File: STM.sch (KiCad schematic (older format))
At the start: 14 parts, among them J3 Micro_SD_Card_Det, J4 TagConnect_TC2030_SWD, Q9 AO3401A, SW8 POWER, U8 STM32L151C8Tx

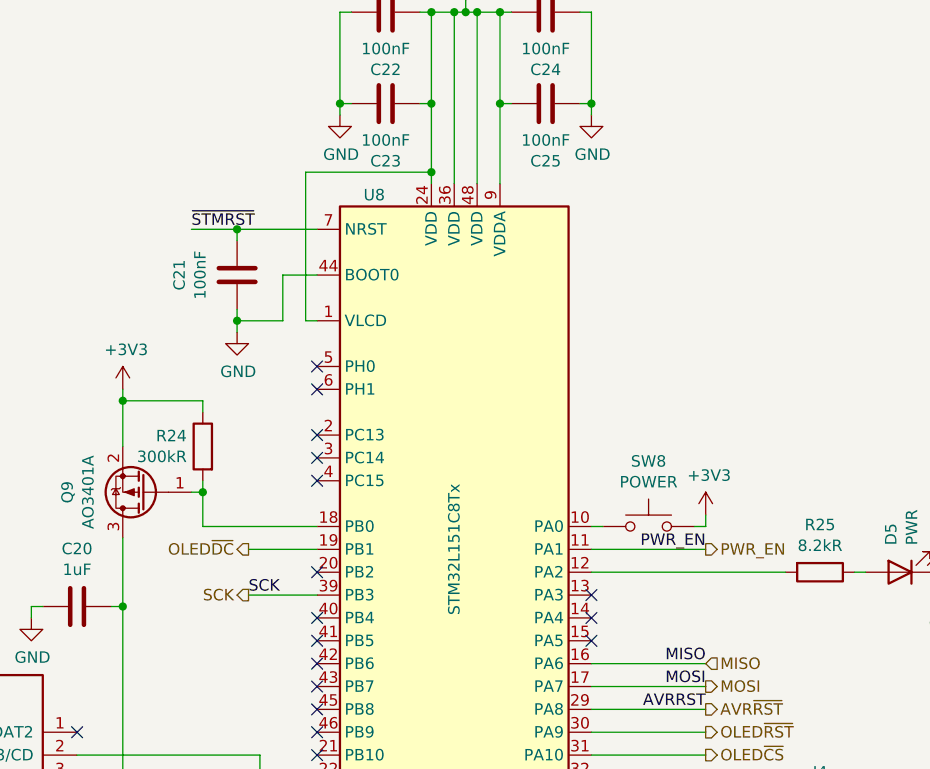
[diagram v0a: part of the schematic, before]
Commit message: Add charge state/current sensing and VBUS wakeup source
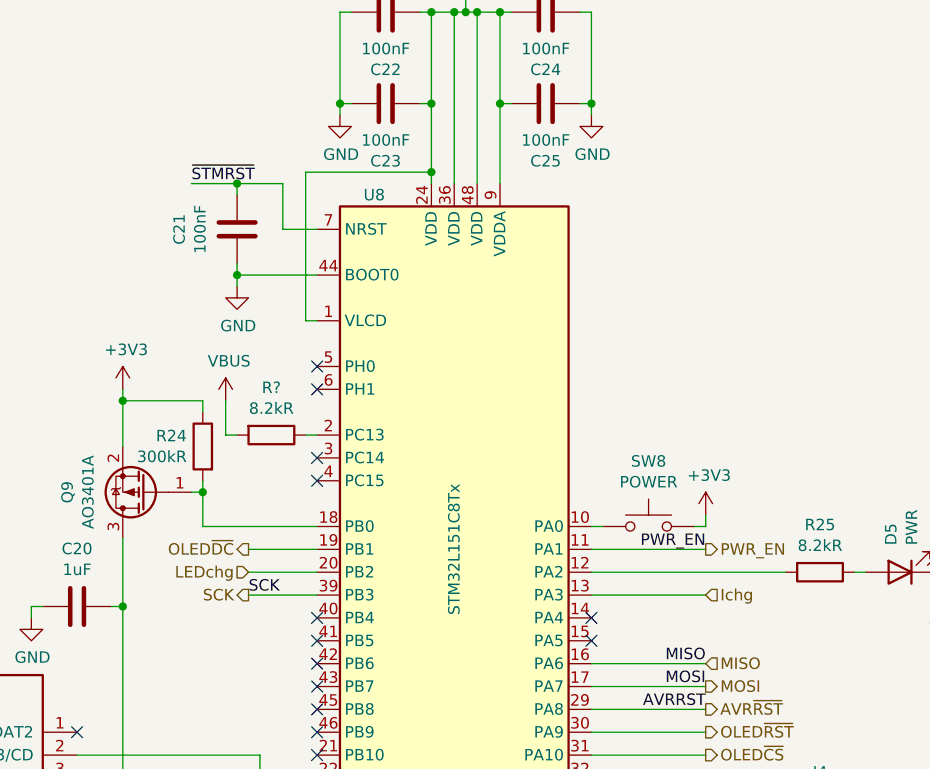
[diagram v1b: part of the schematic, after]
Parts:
- added R?: 8.2kR, Resistor_SMD:R_0402_1005Metric, symbol Device:R
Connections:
- net Ichg: now reaches U8.13 (PA3)
- net at U8.2 (PC13): now also R?.1
- net LEDchg: now reaches U8.20 (PB2)
- new net VBUS: R?.2
- no-connect marks 22 -> 19
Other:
- moved on the sheet: C21
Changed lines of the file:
@@
 L Device:C C?
 U 1 1 60D10135
-P 5100 2700
+P 5100 2500
 AR Path="/60D10135" Ref="C?"  Part="1"
 AR Path="/6051E9DC/60D10135" Ref="C?"  Part="1"
 AR Path="/60CF39C0/60D10135" Ref="C21"  Part="1"
-F 0 "C21" V 5352 2700 50  0000 C CNN
-F 1 "100nF" V 5261 2700 50  0000 C CNN
-F 2 "Capacitor_SMD:C_0402_1005Metric" H 5138 2550 50  0001 C CNN
-F 3 "~" H 5100 2700 50  0001 C CNN
-F 4 "C1525" H 5100 2700 50  0001 C CNN "LCSC"
-	1    5100 2700
+F 0 "C21" V 5352 2500 50  0000 C CNN
+F 1 "100nF" V 5261 2500 50  0000 C CNN
+F 2 "Capacitor_SMD:C_0402_1005Metric" H 5138 2350 50  0001 C CNN
+F 3 "~" H 5100 2500 50  0001 C CNN
+F 4 "C1525" H 5100 2500 50  0001 C CNN "LCSC"
+	1    5100 2500
 	-1   0    0    1
 $EndComp
@@
 L power:GND #PWR?
 U 1 1 60D1013B
-P 5100 2950
+P 5100 2750
 AR Path="/6051E9DC/60D1013B" Ref="#PWR?"  Part="1"
 AR Path="/60CF39C0/60D1013B" Ref="#PWR0105"  Part="1"
-F 0 "#PWR0105" H 5100 2700 50  0001 C CNN
-F 1 "GND" H 5105 2777 50  0000 C CNN
-F 2 "" H 5100 2950 50  0001 C CNN
-F 3 "" H 5100 2950 50  0001 C CNN
-	1    5100 2950
-	1    0    0    -1
-$EndComp
-Wire Wire Line
-	5100 2500 5100 2550
+F 0 "#PWR0105" H 5100 2500 50  0001 C CNN
+F 1 "GND" H 5105 2577 50  0000 C CNN
+F 2 "" H 5100 2750 50  0001 C CNN
+F 3 "" H 5100 2750 50  0001 C CNN
+	1    5100 2750
+	1    0    0    -1
+$EndComp
+Wire Wire Line
+	5100 2300 5100 2350
 $Comp
 L Device:C C?
@@
 Wire Wire Line
 	7150 5200 6650 5200
-Text Label 4900 2500 0    50   ~ 0
+Text Label 4900 2300 0    50   ~ 0
 ~STMRST
 Wire Wire Line
-	4900 2500 5100 2500
-Connection ~ 5100 2500
+	4900 2300 5100 2300
 Text Label 8450 5200 2    50   ~ 0
 ~STMRST
@@
 $EndComp
 Wire Wire Line
-	5100 2850 5100 2900
-Wire Wire Line
-	5450 2700 5300 2700
-Wire Wire Line
-	5300 2700 5300 2900
-Wire Wire Line
-	5300 2900 5100 2900
-Connection ~ 5100 2900
-Wire Wire Line
-	5100 2900 5100 2950
-Wire Wire Line
-	5100 2500 5450 2500
+	5100 2650 5100 2700
+Connection ~ 5100 2700
+Wire Wire Line
+	5100 2700 5100 2750
 $Comp
 L Device:C C?
@@
 NoConn ~ 4400 4700
 NoConn ~ 4400 5400
-NoConn ~ 6650 4100
 NoConn ~ 6650 4200
 NoConn ~ 6650 4900
@@
 NoConn ~ 5450 4300
 NoConn ~ 5450 4200
-NoConn ~ 5450 4000
-NoConn ~ 5450 3400
 Text HLabel 7150 3900 2    50   Output ~ 0
 PWR_EN
@@
 Text HLabel 5150 3900 0    50   Output ~ 0
 OLED~DC
+$Comp
+L power:VBUS #PWR?
+U 1 1 60FE73CC
+P 5050 3250
+F 0 "#PWR?" H 5050 3100 50  0001 C CNN
+F 1 "VBUS" H 5065 3423 50  0000 C CNN
+F 2 "" H 5050 3250 50  0001 C CNN
+F 3 "" H 5050 3250 50  0001 C CNN
+	1    5050 3250
+	1    0    0    -1
+$EndComp
+$Comp
+L Device:R R?
+U 1 1 60FE8A0E
+P 5250 3400
+AR Path="/60FE8A0E" Ref="R?"  Part="1"
+AR Path="/6051E9DC/60FE8A0E" Ref="R?"  Part="1"
+AR Path="/60CF39C0/60FE8A0E" Ref="R?"  Part="1"
+F 0 "R?" V 5043 3400 50  0000 C CNN
+F 1 "8.2kR" V 5134 3400 50  0000 C CNN
+F 2 "Resistor_SMD:R_0402_1005Metric" V 5180 3400 50  0001 C CNN
+F 3 "~" H 5250 3400 50  0001 C CNN
+F 4 "C25924" V 5250 3400 50  0001 C CNN "LCSC"
+	1    5250 3400
+	0    1    1    0
+$EndComp
+Wire Wire Line
+	5400 3400 5450 3400
+Wire Wire Line
+	5450 2500 5300 2500
+Wire Wire Line
+	5300 2500 5300 2300
+Wire Wire Line
+	5300 2300 5100 2300
+Connection ~ 5100 2300
+Wire Wire Line
+	5100 2700 5450 2700
+Wire Wire Line
+	5050 3250 5050 3400
+Wire Wire Line
+	5050 3400 5100 3400
+Wire Wire Line
+	6650 4100 7150 4100
+Text HLabel 7150 4100 2    50   Input ~ 0
+Ichg
+Wire Wire Line
+	5450 4000 5150 4000
+Text HLabel 5150 4000 0    50   Input ~ 0
+LEDchg
 $EndSCHEMATC

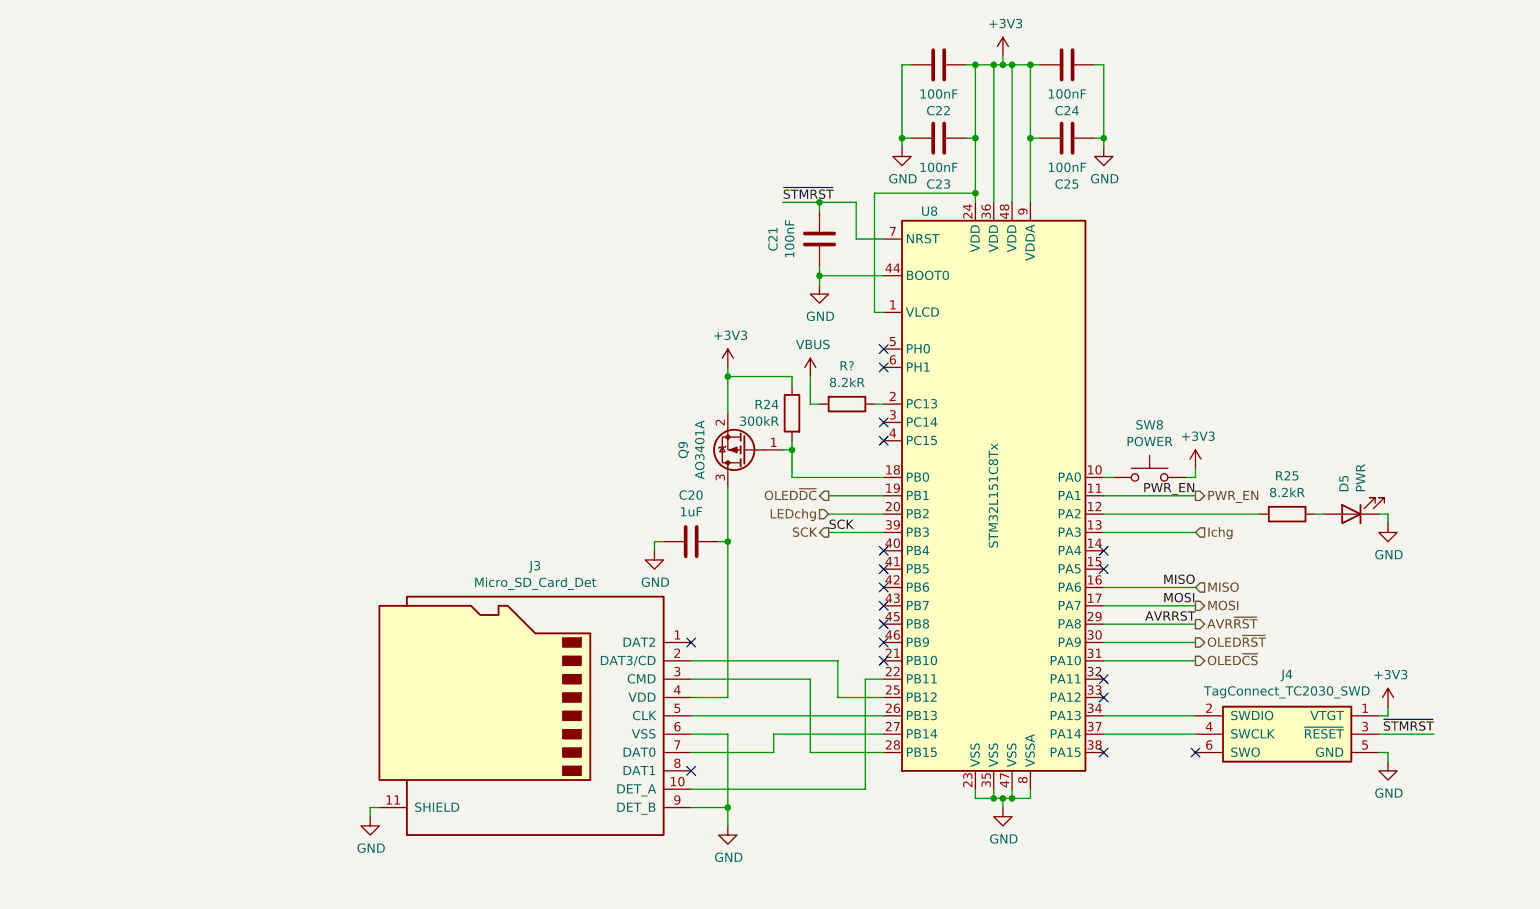
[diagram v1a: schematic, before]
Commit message: Implement fuel gauging
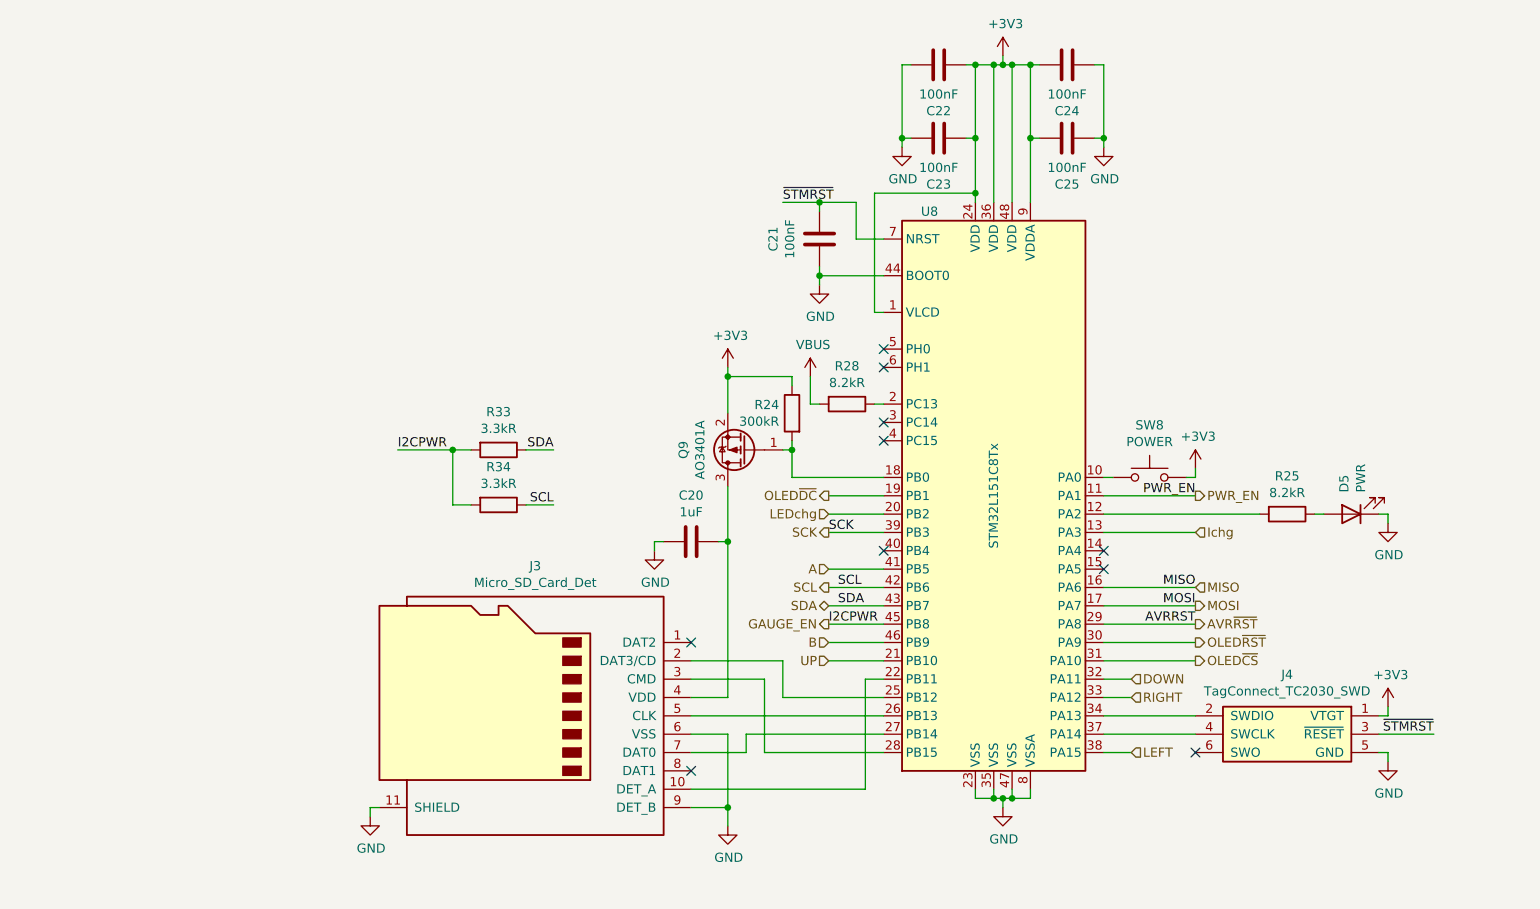
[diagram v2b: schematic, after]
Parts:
- added R33, R34: 3.3kR, Resistor_SMD:R_0402_1005Metric, symbol Device:R
- gave numbers to parts that had none: 1
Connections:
- net UP: now reaches U8.21 (PB10)
- net DOWN: now reaches U8.32 (PA11)
- net RIGHT: now reaches U8.33 (PA12)
- net LEFT: now reaches U8.38 (PA15)
- net A: now reaches U8.41 (PB5)
- net SCL: now reaches U8.42 (PB6)
- net SCL: now also R34.1
- net SDA: now reaches U8.43 (PB7)
- net SDA: now also R33.1
- net GAUGE_EN: now reaches U8.45 (PB8)
- net GAUGE_EN: now also R33.2, R34.2
- net B: now reaches U8.46 (PB9)
- no-connect marks 19 -> 10
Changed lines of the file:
@@
 	5450 5100 4400 5100
 Wire Wire Line
-	5450 5200 4850 5200
-Wire Wire Line
-	4850 5200 4850 5300
-Wire Wire Line
-	4850 5300 4400 5300
-Wire Wire Line
-	5450 5300 5050 5300
-Wire Wire Line
-	5050 5300 5050 4900
-Wire Wire Line
-	5050 4900 4400 4900
-Wire Wire Line
-	4400 4800 5200 4800
-Wire Wire Line
-	5200 4800 5200 5000
-Wire Wire Line
-	5200 5000 5450 5000
+	4400 4800 4900 4800
 $Comp
 L power:GND #PWR?
@@
 NoConn ~ 4400 5400
 NoConn ~ 6650 4200
-NoConn ~ 6650 4900
-NoConn ~ 6650 5000
-NoConn ~ 6650 5300
-NoConn ~ 5450 4800
-NoConn ~ 5450 4700
-NoConn ~ 5450 4600
-NoConn ~ 5450 4500
-NoConn ~ 5450 4400
-NoConn ~ 5450 4300
 NoConn ~ 5450 4200
 Text HLabel 7150 3900 2    50   Output ~ 0
@@
 OLED~DC
 $Comp
-L power:VBUS #PWR?
+L power:VBUS #PWR0103
 U 1 1 60FE73CC
 P 5050 3250
-F 0 "#PWR?" H 5050 3100 50  0001 C CNN
+F 0 "#PWR0103" H 5050 3100 50  0001 C CNN
 F 1 "VBUS" H 5065 3423 50  0000 C CNN
 F 2 "" H 5050 3250 50  0001 C CNN
@@
 AR Path="/60FE8A0E" Ref="R?"  Part="1"
 AR Path="/6051E9DC/60FE8A0E" Ref="R?"  Part="1"
-AR Path="/60CF39C0/60FE8A0E" Ref="R?"  Part="1"
-F 0 "R?" V 5043 3400 50  0000 C CNN
+AR Path="/60CF39C0/60FE8A0E" Ref="R28"  Part="1"
+F 0 "R28" V 5043 3400 50  0000 C CNN
 F 1 "8.2kR" V 5134 3400 50  0000 C CNN
 F 2 "Resistor_SMD:R_0402_1005Metric" V 5180 3400 50  0001 C CNN
@@
 Text HLabel 5150 4000 0    50   Input ~ 0
 LEDchg
+Wire Wire Line
+	5450 4400 5150 4400
+Wire Wire Line
+	5450 4500 5150 4500
+Text HLabel 5150 4400 0    50   Output ~ 0
+SCL
+Text HLabel 5150 4500 0    50   BiDi ~ 0
+SDA
+Text Label 5200 4400 0    50   ~ 0
+SCL
+Text Label 5200 4500 0    50   ~ 0
+SDA
+Wire Wire Line
+	5450 4600 5150 4600
+Text HLabel 5150 4600 0    50   Output ~ 0
+GAUGE_EN
+$Comp
+L Device:R R?
+U 1 1 611AA57E
+P 3350 3650
+AR Path="/611AA57E" Ref="R?"  Part="1"
+AR Path="/60CF39C0/611AA57E" Ref="R33"  Part="1"
+F 0 "R33" V 3143 3650 50  0000 C CNN
+F 1 "3.3kR" V 3234 3650 50  0000 C CNN
+F 2 "Resistor_SMD:R_0402_1005Metric" V 3280 3650 50  0001 C CNN
+F 3 "~" H 3350 3650 50  0001 C CNN
+F 4 "C25890" V 3350 3650 50  0001 C CNN "LCSC"
+	1    3350 3650
+	0    1    1    0
+$EndComp
+Text Label 5150 4600 0    50   ~ 0
+I2CPWR
+$Comp
+L Device:R R?
+U 1 1 611AE5AD
+P 3350 3950
+AR Path="/611AE5AD" Ref="R?"  Part="1"
+AR Path="/60CF39C0/611AE5AD" Ref="R34"  Part="1"
+F 0 "R34" V 3143 3950 50  0000 C CNN
+F 1 "3.3kR" V 3234 3950 50  0000 C CNN
+F 2 "Resistor_SMD:R_0402_1005Metric" V 3280 3950 50  0001 C CNN
+F 3 "~" H 3350 3950 50  0001 C CNN
+F 4 "C25890" V 3350 3950 50  0001 C CNN "LCSC"
+	1    3350 3950
+	0    1    1    0
+$EndComp
+Wire Wire Line
+	3200 3950 3100 3950
+Wire Wire Line
+	3100 3950 3100 3650
+Wire Wire Line
+	3100 3650 3200 3650
+Connection ~ 3100 3650
+Text Label 2800 3650 0    50   ~ 0
+I2CPWR
+Wire Wire Line
+	2800 3650 3100 3650
+Wire Wire Line
+	3500 3650 3650 3650
+Text Label 3650 3650 2    50   ~ 0
+SDA
+Wire Wire Line
+	3500 3950 3650 3950
+Text Label 3650 3950 2    50   ~ 0
+SCL
+Wire Wire Line
+	5450 4300 5150 4300
+Text HLabel 5150 4300 0    50   Input ~ 0
+A
+Wire Wire Line
+	5450 4700 5150 4700
+Text HLabel 5150 4700 0    50   Input ~ 0
+B
+Wire Wire Line
+	4700 5300 4700 5200
+Wire Wire Line
+	4700 5300 4400 5300
+Wire Wire Line
+	4700 5200 5450 5200
+Wire Wire Line
+	4800 5300 4800 4900
+Wire Wire Line
+	4800 5300 5450 5300
+Wire Wire Line
+	4800 4900 4400 4900
+Wire Wire Line
+	4900 4800 4900 5000
+Wire Wire Line
+	4900 5000 5450 5000
+Wire Wire Line
+	5450 4800 5150 4800
+Text HLabel 5150 4800 0    50   Input ~ 0
+UP
+Text HLabel 6800 5300 2    50   Input ~ 0
+LEFT
+Wire Wire Line
+	6800 5300 6650 5300
+Text HLabel 6800 4900 2    50   Input ~ 0
+DOWN
+Wire Wire Line
+	6800 4900 6650 4900
+Text HLabel 6800 5000 2    50   Input ~ 0
+RIGHT
+Wire Wire Line
+	6800 5000 6650 5000
 $EndSCHEMATC

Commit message: Finish layout
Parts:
- D5: footprint Diode_SMD:D_0603_1608Metric -> LED_SMD:LED_0603_1608Metric
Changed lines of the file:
@@
 AR Path="/6051E9DC/60D101E5" Ref="D?"  Part="1"
 AR Path="/60CF39C0/60D101E5" Ref="D5"  Part="1"
-F 0 "D5" V 8039 3882 50  0000 R CNN
-F 1 "PWR" V 7948 3882 50  0000 R CNN
-F 2 "Diode_SMD:D_0603_1608Metric" H 8000 4000 50  0001 C CNN
+F 0 "D5" H 7993 3745 50  0000 C CNN
+F 1 "PWR" H 7993 3836 50  0000 C CNN
+F 2 "LED_SMD:LED_0603_1608Metric" H 8000 4000 50  0001 C CNN
 F 3 "~" H 8000 4000 50  0001 C CNN
 F 4 "C2290" H 8000 4000 50  0001 C CNN "LCSC"
